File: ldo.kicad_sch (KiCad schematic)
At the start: 18 parts, among them Q1 DMG1012T-7, U8 LT3033EUDC_QFN

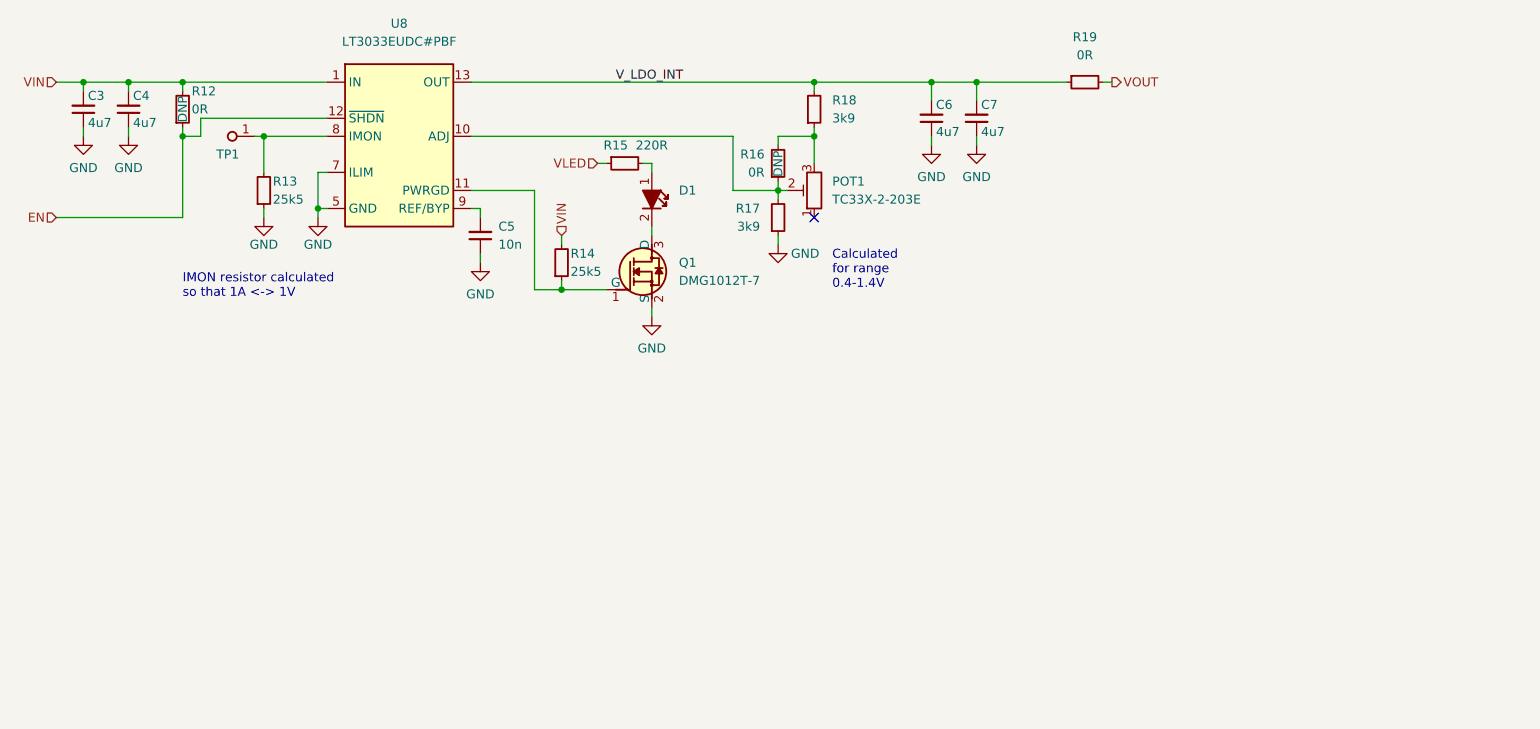
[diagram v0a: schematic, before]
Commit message: [#52835] schematics: update LDO subsheet
LDO subsheet should not contain feedback so that this sheet could be reused
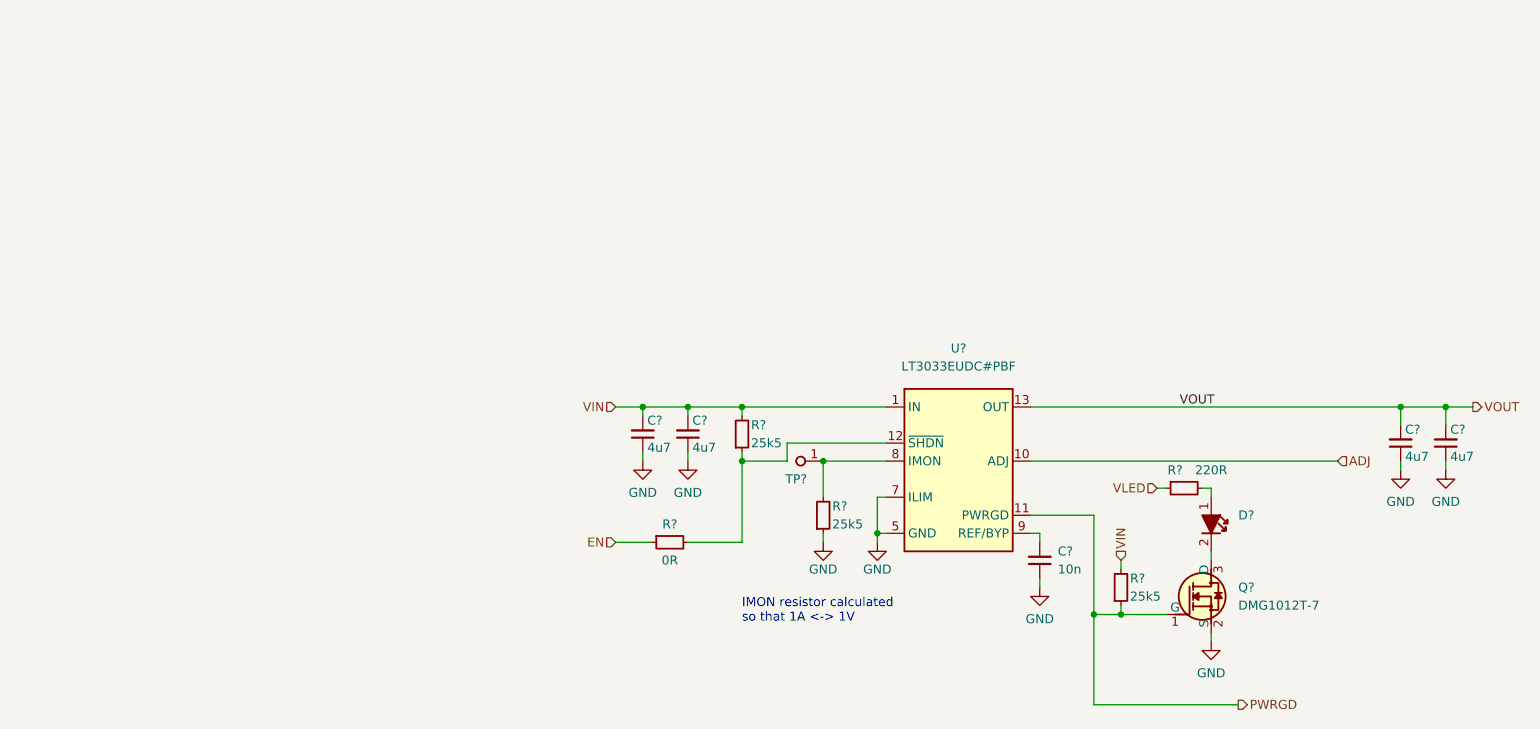
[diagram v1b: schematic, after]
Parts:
- removed C3, C4, C6, C7: C_4u7_0402, antmicro-footprints:C_0402_1005Metric, symbol antmicroCapacitors0402:C_4u7_0402
- removed C5: C_10n_0402, antmicro-footprints:C_0402_1005Metric, symbol antmicroCapacitors0402:C_10n_0402
- removed D1: LED_G_0603_KP-1608CGCK, antmicro-footprints:LED_0603_1608Metric_G, symbol antmicroLEDIndicationDiscrete:LED_G_0603_KP-1608CGCK
- removed POT1: TC33X-2-203E, antmicro-footprints:Trimpot_3.8mmx3.6mm_TC33X-2-103E, symbol antmicroTrimmerPotentiometers:TC33X-2-203E
- removed Q1: DMG1012T-7, antmicro-footprints:SOT-523, symbol antmicroTransistorsFETsMOSFETsSingle:DMG1012T-7
- removed R12, R16, R19: R_0R_0402, antmicro-footprints:R_0402_1005Metric, symbol antmicroResistors0402:R_0R_0402
- removed R13, R14: R_25k5_0402, antmicro-footprints:R_0402_1005Metric, symbol antmicroResistors0402:R_25k5_0402
- removed R15: R_220R_0402, antmicro-footprints:R_0402_1005Metric, symbol antmicroResistors0402:R_220R_0402
- removed R17, R18: R_3k9_0402, antmicro-footprints:R_0402_1005Metric, symbol antmicroResistors0402:R_3k9_0402
- removed TP1: TP_0.75mm_SMD, antmicro-footprints:TP_SMD_0.75mm, symbol antmicroTestPoints:TP_0.75mm_SMD
- removed U8: LT3033EUDC_QFN, antmicro-footprints:QFN-20-4EP_3x4x0.75mm_P0.5mm_Layout4x6_LT3033, symbol antmicroPMICVoltageRegulatorsLinear:LT3033EUDC_QFN
- added C? (x4): C_4u7_0402, antmicro-footprints:C_0402_1005Metric, symbol antmicroCapacitors0402:C_4u7_0402
- added C?: C_10n_0402, antmicro-footprints:C_0402_1005Metric, symbol antmicroCapacitors0402:C_10n_0402
- added D?: LED_G_0603_KP-1608CGCK, antmicro-footprints:LED_0603_1608Metric_G, symbol antmicroLEDIndicationDiscrete:LED_G_0603_KP-1608CGCK
- added Q?: DMG1012T-7, antmicro-footprints:SOT-523, symbol antmicroTransistorsFETsMOSFETsSingle:DMG1012T-7
- added R? (x3): R_25k5_0402, antmicro-footprints:R_0402_1005Metric, symbol antmicroResistors0402:R_25k5_0402
- added R?: R_0R_0402, antmicro-footprints:R_0402_1005Metric, symbol antmicroResistors0402:R_0R_0402
- added R?: R_220R_0402, antmicro-footprints:R_0402_1005Metric, symbol antmicroResistors0402:R_220R_0402
- added TP?: TP_0.75mm_SMD, antmicro-footprints:TP_SMD_0.75mm, symbol antmicroTestPoints:TP_0.75mm_SMD
- added U?: LT3033EUDC_QFN, antmicro-footprints:QFN-20-4EP_3x4x0.75mm_P0.5mm_Layout4x6_LT3033, symbol antmicroPMICVoltageRegulatorsLinear:LT3033EUDC_QFN
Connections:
- net EN: now also R?.1
- net GND: now also C?.1, C?.1, C?.1, C?.1, C?.1, Q?.2 (S), R?.1, U?.5 (GND), U?.6 (GND), U?.7 (ILIM)
- net VIN: now also C?.2, C?.2, R?.2, R?.2, U?.1 (IN), U?.15 (IN), U?.16 (IN), U?.2 (IN), U?.21 (IN), U?.22 (IN)
- net VLED: now also R?.1
- net VOUT: now also C?.2, C?.2, U?.13 (OUT), U?.14 (OUT), U?.17 (OUT), U?.18 (OUT), U?.19 (OUT), U?.20 (OUT), U?.23 (OUT), U?.24 (OUT), U?.3 (OUT), U?.4 (OUT)
- new net: D?.1, R?.2
- new net: D?.2, Q?.3 (D)
- new net: R?.1, R?.2, U?.12 (~{SHDN})
- new net: R?.2, TP?.1, U?.8 (IMON)
- new net: C?.2, U?.9 (REF/BYP)
- new net ADJ: U?.10 (ADJ)
- new net PWRGD: Q?.1 (G), R?.1, U?.11 (PWRGD)
- no-connect marks 1 -> 0
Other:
- note removed: "Calculated for range 0.4-1.4V"

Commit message: Loclib
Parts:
- C? (x4): footprint antmicro-footprints:C_0402_1005Metric -> lpddr5-testbed-footprints:C_0402_1005Metric; symbol antmicroCapacitors0402:C_4u7_0402 -> lpddr5-testbed:C_4u7_0402
- C?: footprint antmicro-footprints:C_0402_1005Metric -> lpddr5-testbed-footprints:C_0402_1005Metric; symbol antmicroCapacitors0402:C_10n_0402 -> lpddr5-testbed:C_10n_0402
- D?: footprint antmicro-footprints:LED_0603_1608Metric_G -> lpddr5-testbed-footprints:LED_0603_1608Metric_G; symbol antmicroLEDIndicationDiscrete:LED_G_0603_KP-1608CGCK -> lpddr5-testbed:LED_G_0603_KP-1608CGCK
- Q?: footprint antmicro-footprints:SOT-523 -> lpddr5-testbed-footprints:SOT-523; symbol antmicroTransistorsFETsMOSFETsSingle:DMG1012T-7 -> lpddr5-testbed:DMG1012T-7
- R? (x3): footprint antmicro-footprints:R_0402_1005Metric -> lpddr5-testbed-footprints:R_0402_1005Metric; symbol antmicroResistors0402:R_25k5_0402 -> lpddr5-testbed:R_25k5_0402
- R?: footprint antmicro-footprints:R_0402_1005Metric -> lpddr5-testbed-footprints:R_0402_1005Metric; symbol antmicroResistors0402:R_0R_0402 -> lpddr5-testbed:R_0R_0402
- R?: footprint antmicro-footprints:R_0402_1005Metric -> lpddr5-testbed-footprints:R_0402_1005Metric; symbol antmicroResistors0402:R_220R_0402 -> lpddr5-testbed:R_220R_0402
- TP?: footprint antmicro-footprints:TP_SMD_0.75mm -> lpddr5-testbed-footprints:TP_SMD_0.75mm; symbol antmicroTestPoints:TP_0.75mm_SMD -> lpddr5-testbed:TP_0.75mm_SMD
- U?: footprint antmicro-footprints:QFN-20-4EP_3x4x0.75mm_P0.5mm_Layout4x6_LT3033 -> lpddr5-testbed-footprints:QFN-20-4EP_3x4x0.75mm_P0.5mm_Layout4x6_LT3033; symbol antmicroPMICVoltageRegulatorsLinear:LT3033EUDC_QFN -> lpddr5-testbed:LT3033EUDC_QFN
